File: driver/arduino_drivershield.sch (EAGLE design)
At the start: 17 parts, among them IC1 LB1973M, IC10 74HC14D, IC11 74HC14D, IC2 LB1973M, IC3 LB1973M, IC4 LB1973M, IC5 LB1973M, IC6 LB1973M, IC7 LB1973M, IC8 LB1973M, IC9 74HC14D, U1 ARDUINO_SHIELDLABEL

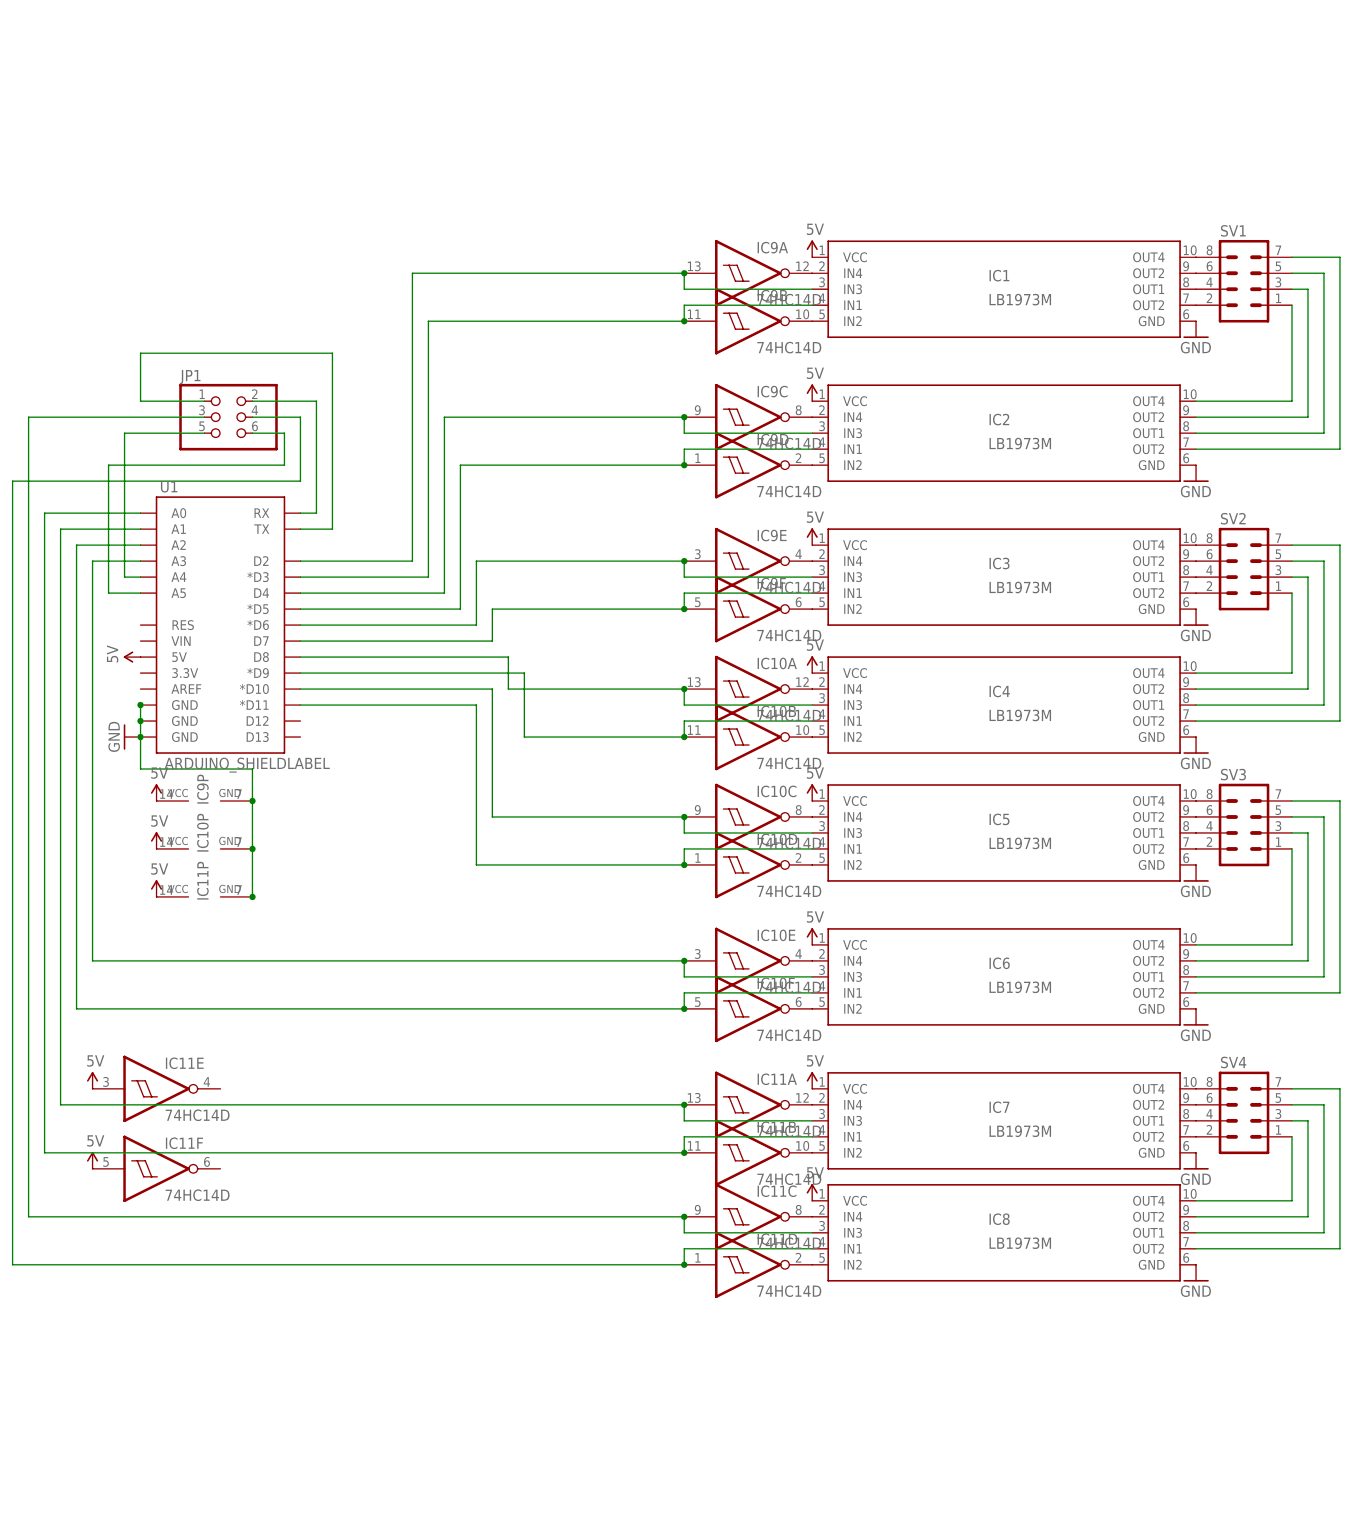
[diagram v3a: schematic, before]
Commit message: adjusted signals a bit, it seems adding one more 7414 will be prudent
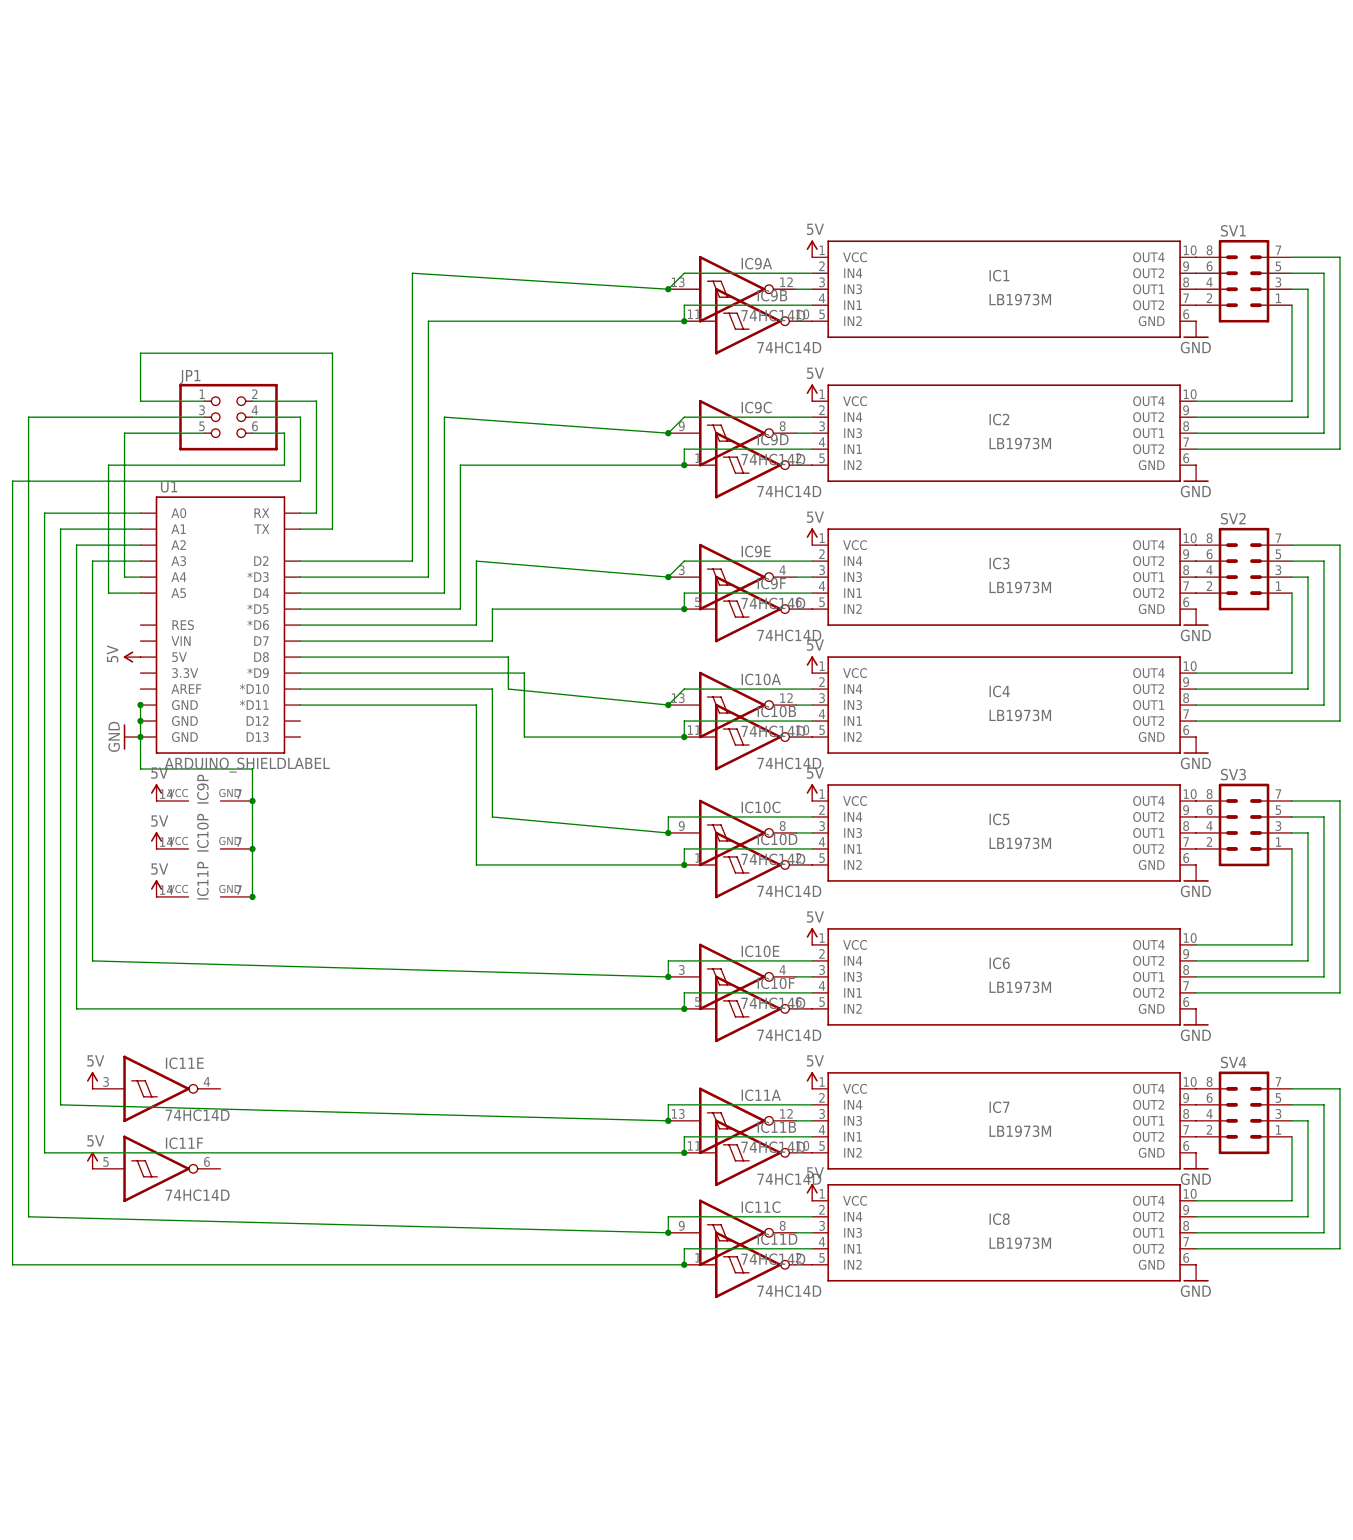
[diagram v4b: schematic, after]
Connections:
- net N$1: now also IC2.IN3, IC9C.O; no longer IC1.IN4, IC9A.O
- net N$15: now also IC3.IN3, IC9E.O; no longer IC10A.O, IC4.IN4
- net N$17: now also IC1.IN4; no longer IC1.IN3
- net N$19: now also IC2.IN4; no longer IC2.IN3
- net N$21: now also IC3.IN4; no longer IC3.IN3
- net N$23: now also IC4.IN4; no longer IC4.IN3
- net N$25: now also IC5.IN4; no longer IC5.IN3
- net N$27: now also IC6.IN4; no longer IC6.IN3
- net N$29: now also IC7.IN4; no longer IC7.IN3
- net N$31: now also IC8.IN4; no longer IC8.IN3
- net N$33: now also IC5.IN3; no longer IC5.IN4
- net N$39: now also IC6.IN3; no longer IC6.IN4
- net N$41: now also IC7.IN3; no longer IC7.IN4
- net N$47: now also IC8.IN3; no longer IC8.IN4
- net N$7: now also IC10A.O, IC4.IN3; no longer IC2.IN4, IC9C.O
- net N$9: now also IC1.IN3, IC9A.O; no longer IC3.IN4, IC9E.O
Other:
- moved on the sheet: IC10A, IC10C, IC10E, IC11A, IC11C, IC9A, IC9C, IC9E

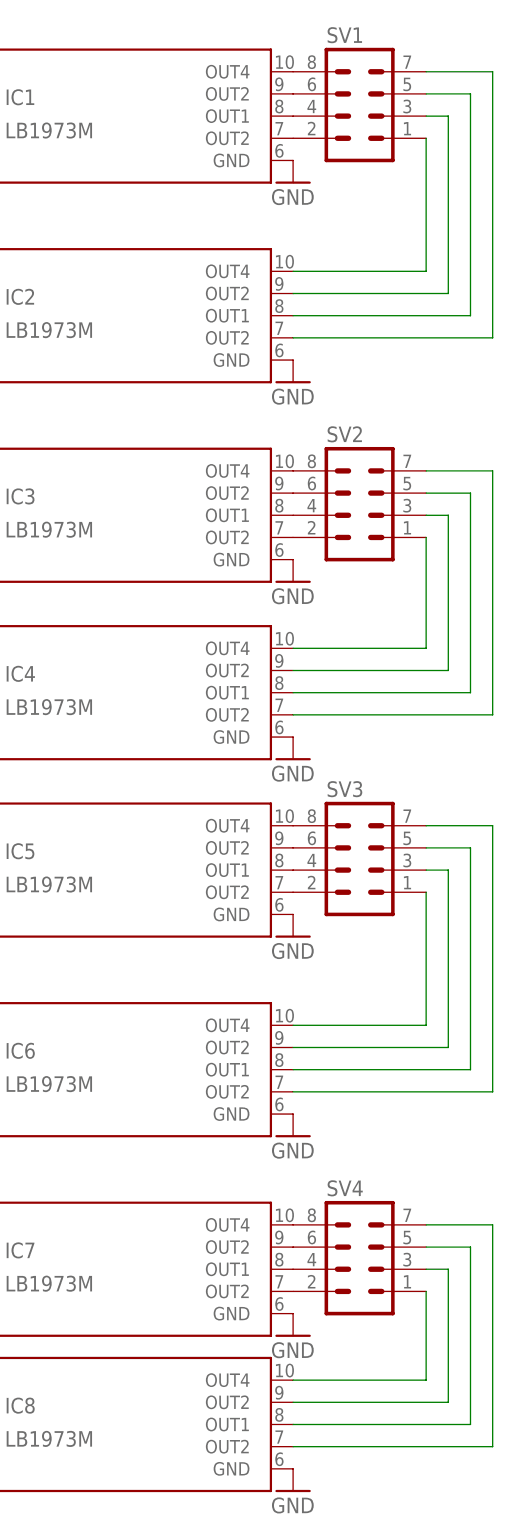
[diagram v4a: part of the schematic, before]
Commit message: switched to SIL connectors for nicer schematic
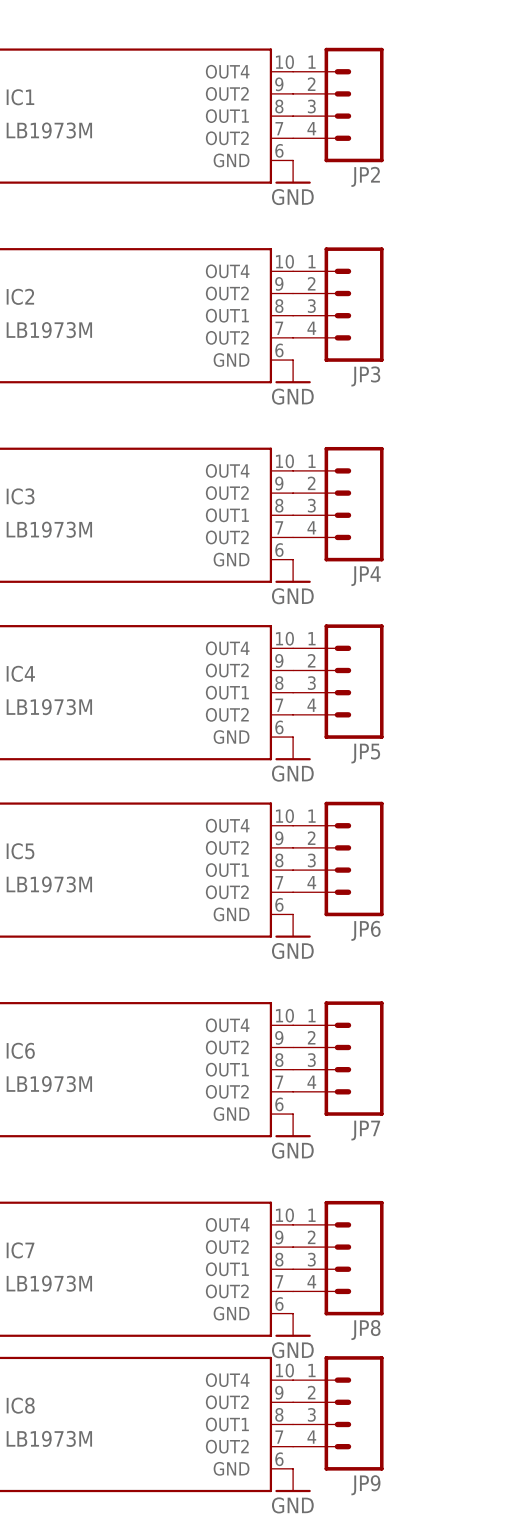
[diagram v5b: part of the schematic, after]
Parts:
- removed SV1, SV2, SV3, SV4: (no value), con-lstb:MA04-2
- added JP2, JP3, JP4, JP5, JP6, JP7, JP8, JP9: (no value), SparkFun-Connectors:M041X04_NO_SILK
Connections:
- net N$11: now also IC2.OUT4, JP3.1; no longer IC3.OUT2, SV2.2
- net N$12: now also IC2.OUT2@1, JP3.2; no longer IC3.OUT1, SV2.4
- net N$13: now also IC2.OUT1, JP3.3; no longer IC3.OUT2@1, SV2.6
- net N$14: now also IC2.OUT2, JP3.4; no longer IC3.OUT4, SV2.8
- net N$3: now also IC1.OUT4, JP2.1; no longer IC1.OUT2, SV1.2
- net N$35: now also IC3.OUT4, JP4.1; no longer IC5.OUT2, SV3.2
- net N$36: now also IC3.OUT2@1, JP4.2; no longer IC5.OUT1, SV3.4
- net N$37: now also IC3.OUT1, JP4.3; no longer IC5.OUT2@1, SV3.6
- net N$38: now also IC3.OUT2, JP4.4; no longer IC5.OUT4, SV3.8
- net N$4: now also IC1.OUT2@1, JP2.2; no longer IC1.OUT1, SV1.4
- net N$43: now also IC4.OUT4, JP5.1; no longer IC7.OUT2, SV4.2
- net N$44: now also IC4.OUT2@1, JP5.2; no longer IC7.OUT1, SV4.4
- net N$45: now also IC4.OUT1, JP5.3; no longer IC7.OUT2@1, SV4.6
- net N$46: now also IC4.OUT2, JP5.4; no longer IC7.OUT4, SV4.8
- net N$49: now also IC5.OUT4, JP6.1; no longer IC8.OUT4, SV4.1
- net N$5: now also IC1.OUT1, JP2.3; no longer IC1.OUT2@1, SV1.6
- net N$50: now also IC5.OUT2@1, JP6.2; no longer IC8.OUT2@1, SV4.3
- net N$51: now also IC5.OUT1, JP6.3; no longer IC8.OUT1, SV4.5
- net N$52: now also IC5.OUT2, JP6.4; no longer IC8.OUT2, SV4.7
- net N$53: now also JP7.1; no longer SV3.1
- net N$54: now also JP7.2; no longer SV3.3
- net N$55: now also JP7.3; no longer SV3.5
- net N$56: now also JP7.4; no longer SV3.7
- net N$57: now also IC7.OUT4, JP8.1; no longer IC4.OUT4, SV2.1
- net N$58: now also IC7.OUT2@1, JP8.2; no longer IC4.OUT2@1, SV2.3
- net N$59: now also IC7.OUT1, JP8.3; no longer IC4.OUT1, SV2.5
- net N$6: now also IC1.OUT2, JP2.4; no longer IC1.OUT4, SV1.8
- net N$60: now also IC7.OUT2, JP8.4; no longer IC4.OUT2, SV2.7
- net N$61: now also IC8.OUT4, JP9.1; no longer IC2.OUT4, SV1.1
- net N$62: now also IC8.OUT2@1, JP9.2; no longer IC2.OUT2@1, SV1.3
- net N$63: now also IC8.OUT1, JP9.3; no longer IC2.OUT1, SV1.5
- net N$64: now also IC8.OUT2, JP9.4; no longer IC2.OUT2, SV1.7

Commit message: starting over...
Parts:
- removed IC10, IC11, IC9: 74HC14D, 74xx-eu:74HC14D
- removed IC3, IC4, IC5, IC6, IC7, IC8: LB1973M, LB1973M:LB1973M
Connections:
- removed net N$1 (its old number): IC2.IN3, IC9C.O
- removed net N$10: IC3.IN2, IC9F.O
- removed net N$15: IC3.IN3, IC9E.O
- removed net N$16: IC10B.O, IC4.IN2
- removed net N$17: IC1.IN4, IC9A.I, U1.D2
- removed net N$18: IC1.IN1, IC9B.I, U1.*D3
- removed net N$19: IC2.IN4, IC9C.I, U1.D4
- removed net N$2 (its old number): IC1.IN2, IC9B.O
- removed net N$20: IC2.IN1, IC9D.I, U1.*D5
- removed net N$21: IC3.IN4, IC9E.I, U1.*D6
- removed net N$22: IC3.IN1, IC9F.I, U1.D7
- removed net N$23: IC10A.I, IC4.IN4, U1.D8
- removed net N$24: IC10B.I, IC4.IN1, U1.*D9
- removed net N$25: IC10C.I, IC5.IN4, U1.*D10
- removed net N$26: IC10D.I, IC5.IN1, U1.*D11
- removed net N$33: IC10C.O, IC5.IN3
- removed net N$34: IC10D.O, IC5.IN2
- removed net N$35: IC3.OUT4, JP4.1
- removed net N$36: IC3.OUT2@1, JP4.2
- removed net N$37: IC3.OUT1, JP4.3
- removed net N$38: IC3.OUT2, JP4.4
- removed net N$39: IC10E.O, IC6.IN3
- removed net N$40: IC10F.O, IC6.IN2
- removed net N$41: IC11A.O, IC7.IN3
- removed net N$42: IC11B.O, IC7.IN2
- removed net N$43: IC4.OUT4, JP5.1
- removed net N$44: IC4.OUT2@1, JP5.2
- removed net N$45: IC4.OUT1, JP5.3
- removed net N$46: IC4.OUT2, JP5.4
- removed net N$47: IC11C.O, IC8.IN3
- removed net N$48: IC11D.O, IC8.IN2
- removed net N$49: IC5.OUT4, JP6.1
- removed net N$50: IC5.OUT2@1, JP6.2
- removed net N$51: IC5.OUT1, JP6.3
- removed net N$52: IC5.OUT2, JP6.4
- removed net N$53: IC6.OUT4, JP7.1
- removed net N$54: IC6.OUT2@1, JP7.2
- removed net N$55: IC6.OUT1, JP7.3
- removed net N$56: IC6.OUT2, JP7.4
- removed net N$57: IC7.OUT4, JP8.1
- removed net N$58: IC7.OUT2@1, JP8.2
- removed net N$59: IC7.OUT1, JP8.3
- removed net N$60: IC7.OUT2, JP8.4
- removed net N$61: IC8.OUT4, JP9.1
- removed net N$62: IC8.OUT2@1, JP9.2
- removed net N$63: IC8.OUT1, JP9.3
- removed net N$64: IC8.OUT2, JP9.4
- removed net N$7 (its old number): IC10A.O, IC4.IN3
- removed net N$8 (its old number): IC2.IN2, IC9D.O
- removed net N$9: IC1.IN3, IC9A.O
- net 5V: no longer IC1.VCC, IC10P.VCC, IC11E.I, IC11F.I, IC11P.VCC, IC2.VCC, IC3.VCC, IC4.VCC, IC5.VCC, IC6.VCC, IC7.VCC, IC8.VCC, IC9P.VCC
- net GND: no longer IC10P.GND, IC11P.GND, IC3.GND, IC4.GND, IC5.GND, IC6.GND, IC7.GND, IC8.GND, IC9P.GND
- net N$27: no longer IC10E.I, IC6.IN4
- net N$28: no longer IC10F.I, IC6.IN1
- net N$29: no longer IC11A.I, IC7.IN4
- net N$30: no longer IC11B.I, IC7.IN1
- net N$31: no longer IC11C.I, IC8.IN4
- net N$32: no longer IC11D.I, IC8.IN1

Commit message: this seems to be a good way, two h-bridges to one 7414
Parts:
- added IC3: 74HC14D, 74xx-eu:74HC14D
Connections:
- new net N$10: IC1.IN2, IC3B.O
- new net N$11: IC2.IN3, IC3E.O
- new net N$12: IC2.IN2, IC3F.O
- new net N$13: IC1.IN1, IC3B.I, U1.*D3
- new net N$14: IC1.IN4, IC3A.I, U1.D2
- new net N$15: IC2.IN4, IC3E.I, U1.D4
- new net N$16: IC2.IN1, IC3F.I, U1.*D5
- new net N$9: IC1.IN3, IC3A.O
- net 5V: now also IC3C.I, IC3D.I, IC3P.VCC
- net GND: now also IC3P.GND
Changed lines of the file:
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@@
 <part name="IC1" library="LB1973M" deviceset="LB1973M" device=""/>
 <part name="IC2" library="LB1973M" deviceset="LB1973M" device=""/>
+<part name="IC3" library="74xx-eu" deviceset="74*14" device="D" technology="HC"/>
+<part name="GND10" library="SparkFun-Aesthetics" deviceset="GND" device=""/>
+<part name="U$2" library="SparkFun-Aesthetics" deviceset="5V" device=""/>
 </parts>
 <sheets>
@@
 <instance part="IC1" gate="G$1" x="149.86" y="83.82"/>
 <instance part="IC2" gate="G$1" x="149.86" y="60.96"/>
+<instance part="IC3" gate="A" x="109.22" y="83.82"/>
+<instance part="IC3" gate="B" x="109.22" y="78.74"/>
+<instance part="IC3" gate="E" x="109.22" y="60.96"/>
+<instance part="IC3" gate="F" x="109.22" y="55.88"/>
+<instance part="IC3" gate="C" x="68.58" y="121.92"/>
+<instance part="IC3" gate="D" x="68.58" y="111.76"/>
+<instance part="IC3" gate="P" x="58.42" y="104.14"/>
+<instance part="GND10" gate="1" x="55.88" y="96.52" rot="R270"/>
+<instance part="U$2" gate="G$1" x="58.42" y="111.76" rot="R90"/>
 </instances>
 <busses>
@@
 <pinref part="U1" gate="G$1" pin="5V"/>
 <pinref part="U$1" gate="G$1" pin="5V"/>
+</segment>
+<segment>
+<pinref part="IC3" gate="D" pin="I"/>
+<pinref part="IC3" gate="P" pin="VCC"/>
+<pinref part="U$2" gate="G$1" pin="5V"/>
+<junction x="58.42" y="111.76"/>
+<pinref part="U$2" gate="G$1" pin="5V"/>
+<pinref part="IC3" gate="C" pin="I"/>
+<wire x1="58.42" y1="121.92" x2="58.42" y2="111.76" width="0.1524" layer="91"/>
 </segment>
 </net>
@@
 <pinref part="IC2" gate="G$1" pin="GND"/>
 </segment>
+<segment>
+<pinref part="IC3" gate="P" pin="GND"/>
+<pinref part="GND10" gate="1" pin="GND"/>
+</segment>
 </net>
 <net name="N$27" class="0">
@@
 </segment>
 </net>
+<net name="N$9" class="0">
+<segment>
+<pinref part="IC1" gate="G$1" pin="IN3"/>
+<pinref part="IC3" gate="A" pin="O"/>
+</segment>
+</net>
+<net name="N$10" class="0">
+<segment>
+<pinref part="IC1" gate="G$1" pin="IN2"/>
+<pinref part="IC3" gate="B" pin="O"/>
+</segment>
+</net>
+<net name="N$13" class="0">
+<segment>
+<pinref part="IC1" gate="G$1" pin="IN1"/>
+<pinref part="IC3" gate="B" pin="I"/>
+<wire x1="119.38" y1="81.28" x2="99.06" y2="81.28" width="0.1524" layer="91"/>
+<wire x1="99.06" y1="81.28" x2="99.06" y2="78.74" width="0.1524" layer="91"/>
+<wire x1="99.06" y1="78.74" x2="55.88" y2="78.74" width="0.1524" layer="91"/>
+<wire x1="55.88" y1="78.74" x2="55.88" y2="38.1" width="0.1524" layer="91"/>
+<pinref part="U1" gate="G$1" pin="*D3"/>
+<wire x1="55.88" y1="38.1" x2="38.1" y2="38.1" width="0.1524" layer="91"/>
+<junction x="99.06" y="78.74"/>
+</segment>
+</net>
+<net name="N$14" class="0">
+<segment>
+<pinref part="IC1" gate="G$1" pin="IN4"/>
+<pinref part="IC3" gate="A" pin="I"/>
+<wire x1="119.38" y1="86.36" x2="99.06" y2="86.36" width="0.1524" layer="91"/>
+<wire x1="99.06" y1="86.36" x2="99.06" y2="83.82" width="0.1524" layer="91"/>
+<pinref part="U1" gate="G$1" pin="D2"/>
+<wire x1="38.1" y1="40.64" x2="53.34" y2="40.64" width="0.1524" layer="91"/>
+<wire x1="53.34" y1="40.64" x2="53.34" y2="83.82" width="0.1524" layer="91"/>
+<wire x1="53.34" y1="83.82" x2="99.06" y2="83.82" width="0.1524" layer="91"/>
+<junction x="99.06" y="83.82"/>
+</segment>
+</net>
+<net name="N$15" class="0">
+<segment>
+<pinref part="IC2" gate="G$1" pin="IN4"/>
+<wire x1="119.38" y1="63.5" x2="99.06" y2="63.5" width="0.1524" layer="91"/>
+<wire x1="99.06" y1="63.5" x2="99.06" y2="60.96" width="0.1524" layer="91"/>
+<pinref part="IC3" gate="E" pin="I"/>
+<pinref part="U1" gate="G$1" pin="D4"/>
+<wire x1="38.1" y1="35.56" x2="58.42" y2="35.56" width="0.1524" layer="91"/>
+<wire x1="58.42" y1="35.56" x2="58.42" y2="60.96" width="0.1524" layer="91"/>
+<wire x1="58.42" y1="60.96" x2="99.06" y2="60.96" width="0.1524" layer="91"/>
+<junction x="99.06" y="60.96"/>
+</segment>
+</net>
+<net name="N$16" class="0">
+<segment>
+<wire x1="99.06" y1="58.42" x2="99.06" y2="55.88" width="0.1524" layer="91"/>
+<pinref part="IC3" gate="F" pin="I"/>
+<pinref part="IC2" gate="G$1" pin="IN1"/>
+<wire x1="119.38" y1="58.42" x2="99.06" y2="58.42" width="0.1524" layer="91"/>
+<wire x1="99.06" y1="55.88" x2="60.96" y2="55.88" width="0.1524" layer="91"/>
+<wire x1="60.96" y1="55.88" x2="60.96" y2="33.02" width="0.1524" layer="91"/>
+<pinref part="U1" gate="G$1" pin="*D5"/>
+<wire x1="60.96" y1="33.02" x2="38.1" y2="33.02" width="0.1524" layer="91"/>
+<junction x="99.06" y="55.88"/>
+</segment>
+</net>
+<net name="N$11" class="0">
+<segment>
+<pinref part="IC2" gate="G$1" pin="IN3"/>
+<pinref part="IC3" gate="E" pin="O"/>
+</segment>
+</net>
+<net name="N$12" class="0">
+<segment>
+<pinref part="IC2" gate="G$1" pin="IN2"/>
+<pinref part="IC3" gate="F" pin="O"/>
+</segment>
+</net>
